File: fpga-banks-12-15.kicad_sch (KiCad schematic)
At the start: 1 part, among them U15 XC7K160T-FFG676

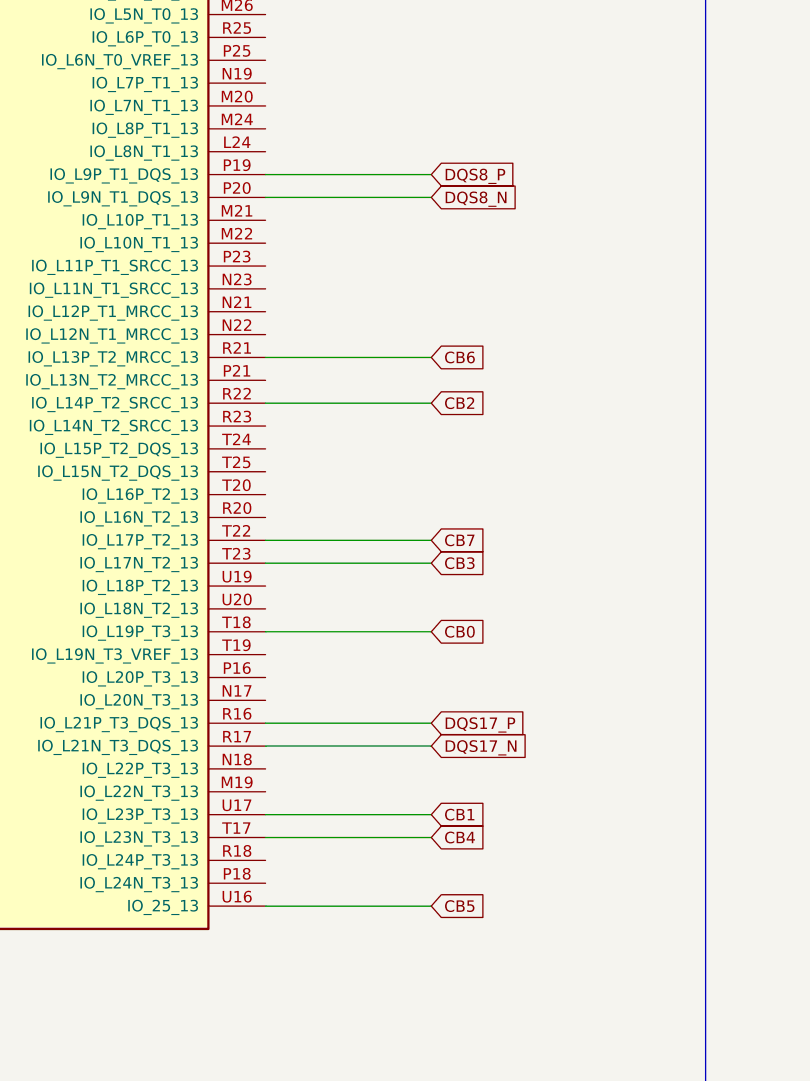
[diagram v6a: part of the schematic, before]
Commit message: Add missing FMC vias, route: MODE, JTAG, active discharge, reconnect 5V buses
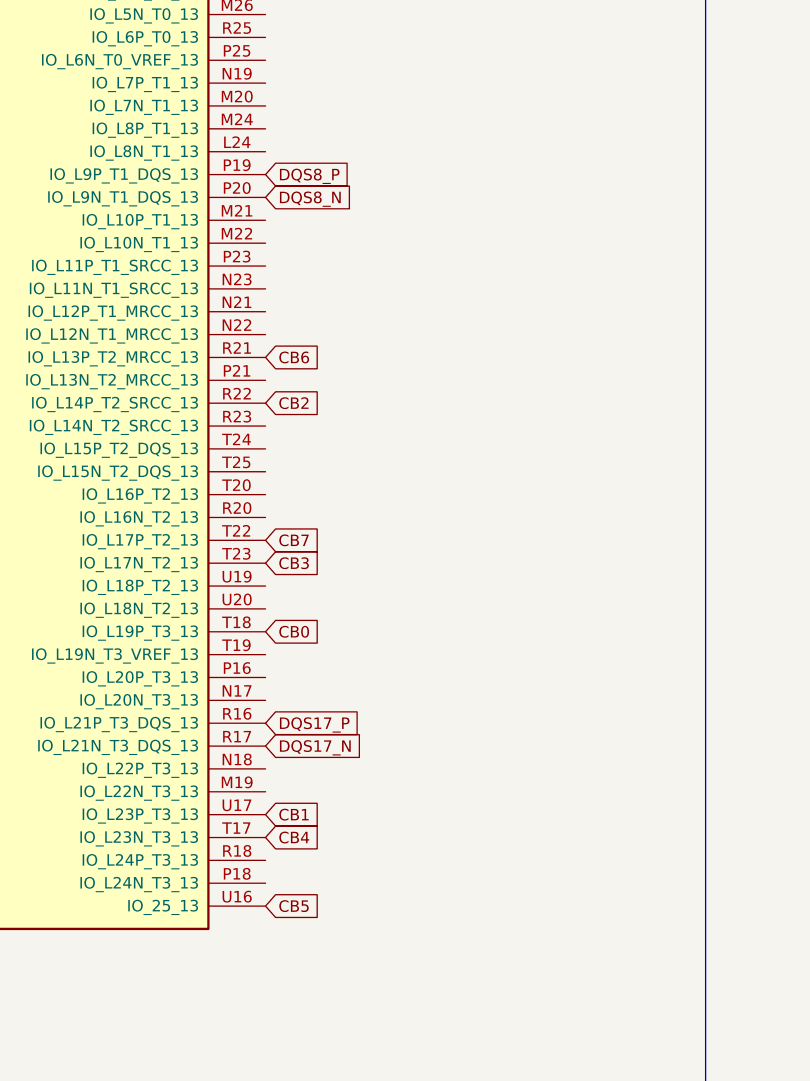
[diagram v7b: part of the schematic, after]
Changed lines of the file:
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@@
     (stroke (width 0) (type default) (color 0 0 0 0))
   )
-  (wire (pts (xy 161.29 208.915) (xy 179.705 208.915))
-    (stroke (width 0) (type default) (color 0 0 0 0))
-  )
   (wire (pts (xy 332.105 72.39) (xy 332.105 66.675))
     (stroke (width 0) (type default) (color 0 0 0 0))
@@
     (stroke (width 0) (type default) (color 0 0 0 0))
   )
-  (wire (pts (xy 161.29 155.575) (xy 179.705 155.575))
-    (stroke (width 0) (type default) (color 0 0 0 0))
-  )
-  (wire (pts (xy 161.29 135.255) (xy 179.705 135.255))
-    (stroke (width 0) (type default) (color 0 0 0 0))
-  )
   (wire (pts (xy 140.97 66.04) (xy 143.51 66.04))
     (stroke (width 0) (type default) (color 0 0 0 0))
   )
-  (wire (pts (xy 161.29 198.755) (xy 179.705 198.755))
-    (stroke (width 0) (type default) (color 0 0 0 0))
-  )
   (wire (pts (xy 82.55 66.04) (xy 85.09 66.04))
     (stroke (width 0) (type default) (color 0 0 0 0))
@@
     (stroke (width 0) (type default) (color 0 0 0 0))
   )
-  (wire (pts (xy 161.29 186.055) (xy 179.705 186.055))
-    (stroke (width 0) (type default) (color 0 0 0 0))
-  )
   (wire (pts (xy 74.93 71.755) (xy 74.93 66.04))
     (stroke (width 0) (type default) (color 0 0 0 0))
@@
     (stroke (width 0) (type default) (color 0 0 0 0))
   )
-  (wire (pts (xy 161.29 216.535) (xy 179.705 216.535))
-    (stroke (width 0) (type default) (color 0 0 0 0))
-  )
   (wire (pts (xy 151.13 71.755) (xy 151.13 66.04))
     (stroke (width 0) (type default) (color 0 0 0 0))
@@
     (stroke (width 0) (type default) (color 0 0 0 0))
   )
-  (wire (pts (xy 161.29 137.795) (xy 179.705 137.795))
-    (stroke (width 0) (type default) (color 0 0 0 0))
-  )
   (wire (pts (xy 348.615 60.96) (xy 348.615 66.675))
     (stroke (width 0) (type default) (color 0 0 0 0))
@@
     (stroke (width 0) (type default) (color 0 0 0 0))
   )
-  (wire (pts (xy 161.29 175.895) (xy 179.705 175.895))
-    (stroke (width 0) (type default) (color 0 0 0 0))
-  )
   (wire (pts (xy 88.9 66.04) (xy 88.9 62.23))
     (stroke (width 0) (type default) (color 0 0 0 0))
@@
     (stroke (width 0) (type default) (color 0 0 0 0))
   )
-  (wire (pts (xy 161.29 178.435) (xy 179.705 178.435))
-    (stroke (width 0) (type default) (color 0 0 0 0))
-  )
   (wire (pts (xy 72.39 66.04) (xy 74.93 66.04))
     (stroke (width 0) (type default) (color 0 0 0 0))
@@
     (stroke (width 0) (type default) (color 0 0 0 0))
   )
-  (wire (pts (xy 161.29 196.215) (xy 179.705 196.215))
-    (stroke (width 0) (type default) (color 0 0 0 0))
-  )
   (wire (pts (xy 154.94 60.96) (xy 154.94 66.04))
     (stroke (width 0) (type default) (color 0 0 0 0))
@@
     (stroke (width 0) (type default) (color 0 0 0 0))
   )
-  (wire (pts (xy 161.29 160.655) (xy 179.705 160.655))
-    (stroke (width 0) (type default) (color 0 0 0 0))
-  )
   (wire (pts (xy 266.065 72.39) (xy 266.065 66.675))
     (stroke (width 0) (type default) (color 0 0 0 0))
   )
-  (wire (pts (xy 161.29 206.375) (xy 179.705 206.375))
-    (stroke (width 0) (type default) (color 0 0 0 0))
-  )
   (image (at 74.295 271.78) (scale 0.15)
     (data
@@
     )
   )
-  (global_label "CB6" (shape input) (at 179.705 155.575 0) (fields_autoplaced)
+  (global_label "CB6" (shape input) (at 161.29 155.575 0) (fields_autoplaced)
     (effects (font (size 1.27 1.27)) (justify left))
-    (property "Intersheet References" "${INTERSHEET_REFS}" (id 0) (at -192.405 -38.1 0)
+    (property "Intersheet References" "${INTERSHEET_REFS}" (id 0) (at -210.82 -38.1 0)
       (effects (font (size 1.27 1.27)) hide)
     )
@@
     )
   )
-  (global_label "CB5" (shape input) (at 179.705 216.535 0) (fields_autoplaced)
+  (global_label "CB5" (shape input) (at 161.29 216.535 0) (fields_autoplaced)
     (effects (font (size 1.27 1.27)) (justify left))
-    (property "Intersheet References" "${INTERSHEET_REFS}" (id 0) (at -192.405 27.94 0)
+    (property "Intersheet References" "${INTERSHEET_REFS}" (id 0) (at -210.82 27.94 0)
       (effects (font (size 1.27 1.27)) hide)
     )
@@
     )
   )
-  (global_label "CB0" (shape input) (at 179.705 186.055 0) (fields_autoplaced)
+  (global_label "CB0" (shape input) (at 161.29 186.055 0) (fields_autoplaced)
     (effects (font (size 1.27 1.27)) (justify left))
-    (property "Intersheet References" "${INTERSHEET_REFS}" (id 0) (at -192.405 -12.7 0)
+    (property "Intersheet References" "${INTERSHEET_REFS}" (id 0) (at -210.82 -12.7 0)
       (effects (font (size 1.27 1.27)) hide)
     )
@@
     )
   )
-  (global_label "CB7" (shape input) (at 179.705 175.895 0) (fields_autoplaced)
+  (global_label "CB7" (shape input) (at 161.29 175.895 0) (fields_autoplaced)
     (effects (font (size 1.27 1.27)) (justify left))
-    (property "Intersheet References" "${INTERSHEET_REFS}" (id 0) (at -192.405 5.08 0)
+    (property "Intersheet References" "${INTERSHEET_REFS}" (id 0) (at -210.82 5.08 0)
       (effects (font (size 1.27 1.27)) hide)
     )
@@
     )
   )
-  (global_label "DQS17_N" (shape input) (at 179.705 198.755 0) (fields_autoplaced)
+  (global_label "DQS17_N" (shape input) (at 161.29 198.755 0) (fields_autoplaced)
     (effects (font (size 1.27 1.27)) (justify left))
-    (property "Intersheet References" "${INTERSHEET_REFS}" (id 0) (at 190.5563 198.6756 0)
+    (property "Intersheet References" "${INTERSHEET_REFS}" (id 0) (at 172.1413 198.6756 0)
       (effects (font (size 1.27 1.27)) (justify left) hide)
     )
@@
     )
   )
-  (global_label "DQS8_N" (shape input) (at 179.705 137.795 0) (fields_autoplaced)
+  (global_label "DQS8_N" (shape input) (at 161.29 137.795 0) (fields_autoplaced)
     (effects (font (size 1.27 1.27)) (justify left))
-    (property "Intersheet References" "${INTERSHEET_REFS}" (id 0) (at 189.3468 137.7156 0)
+    (property "Intersheet References" "${INTERSHEET_REFS}" (id 0) (at 170.9318 137.7156 0)
       (effects (font (size 1.27 1.27)) (justify left) hide)
     )
@@
     )
   )
-  (global_label "CB4" (shape input) (at 179.705 208.915 0) (fields_autoplaced)
+  (global_label "CB4" (shape input) (at 161.29 208.915 0) (fields_autoplaced)
     (effects (font (size 1.27 1.27)) (justify left))
-    (property "Intersheet References" "${INTERSHEET_REFS}" (id 0) (at -192.405 7.62 0)
+    (property "Intersheet References" "${INTERSHEET_REFS}" (id 0) (at -210.82 7.62 0)
       (effects (font (size 1.27 1.27)) hide)
     )
@@
     )
   )
-  (global_label "CB2" (shape input) (at 179.705 160.655 0) (fields_autoplaced)
+  (global_label "CB2" (shape input) (at 161.29 160.655 0) (fields_autoplaced)
     (effects (font (size 1.27 1.27)) (justify left))
-    (property "Intersheet References" "${INTERSHEET_REFS}" (id 0) (at -192.405 -7.62 0)
+    (property "Intersheet References" "${INTERSHEET_REFS}" (id 0) (at -210.82 -7.62 0)
       (effects (font (size 1.27 1.27)) hide)
     )
@@
     )
   )
-  (global_label "DQS17_P" (shape input) (at 179.705 196.215 0) (fields_autoplaced)
+  (global_label "DQS17_P" (shape input) (at 161.29 196.215 0) (fields_autoplaced)
     (effects (font (size 1.27 1.27)) (justify left))
-    (property "Intersheet References" "${INTERSHEET_REFS}" (id 0) (at 190.4959 196.1356 0)
+    (property "Intersheet References" "${INTERSHEET_REFS}" (id 0) (at 172.0809 196.1356 0)
       (effects (font (size 1.27 1.27)) (justify left) hide)
     )
@@
     )
   )
-  (global_label "CB1" (shape input) (at 179.705 206.375 0) (fields_autoplaced)
+  (global_label "CB1" (shape input) (at 161.29 206.375 0) (fields_autoplaced)
     (effects (font (size 1.27 1.27)) (justify left))
-    (property "Intersheet References" "${INTERSHEET_REFS}" (id 0) (at -192.405 10.16 0)
+    (property "Intersheet References" "${INTERSHEET_REFS}" (id 0) (at -210.82 10.16 0)
       (effects (font (size 1.27 1.27)) hide)
     )
@@
     )
   )
-  (global_label "CB3" (shape input) (at 179.705 178.435 0) (fields_autoplaced)
+  (global_label "CB3" (shape input) (at 161.29 178.435 0) (fields_autoplaced)
     (effects (font (size 1.27 1.27)) (justify left))
-    (property "Intersheet References" "${INTERSHEET_REFS}" (id 0) (at -192.405 17.78 0)
+    (property "Intersheet References" "${INTERSHEET_REFS}" (id 0) (at -210.82 17.78 0)
       (effects (font (size 1.27 1.27)) hide)
     )
@@
     )
   )
-  (global_label "DQS8_P" (shape input) (at 179.705 135.255 0) (fields_autoplaced)
+  (global_label "DQS8_P" (shape input) (at 161.29 135.255 0) (fields_autoplaced)
     (effects (font (size 1.27 1.27)) (justify left))
-    (property "Intersheet References" "${INTERSHEET_REFS}" (id 0) (at 189.2863 135.1756 0)
+    (property "Intersheet References" "${INTERSHEET_REFS}" (id 0) (at 170.8713 135.1756 0)
       (effects (font (size 1.27 1.27)) (justify left) hide)
     )
